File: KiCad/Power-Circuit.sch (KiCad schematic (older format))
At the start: 12 parts, among them P12 M20-9980346, P24 M20-9980346

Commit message: controller board schematic complete
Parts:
- gave numbers to parts that had none: 10
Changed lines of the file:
@@
 $Descr A4 11693 8268
 encoding utf-8
-Sheet 5 5
+Sheet 5 6
 Title ""
 Date ""
@@
 MainsLive
 $Comp
-L FUSE F?
+L FUSE F1
 U 1 1 5682385A
 P 2850 2500
-F 0 "F?" H 2850 2650 50  0000 C CNN
+F 0 "F1" H 2850 2650 50  0000 C CNN
 F 1 "83100000005" H 2850 2350 50  0000 C CNN
 F 2 "" H 2850 2500 50  0000 C CNN
@@
 $EndComp
 $Comp
-L VPP24-830 T?
+L VPP24-830 T1
 U 1 1 568240FC
 P 2900 4400
-F 0 "T?" H 2900 5125 50  0000 C CNN
+F 0 "T1" H 2900 5125 50  0000 C CNN
 F 1 "VPP24-830" H 2900 5025 50  0000 C CNN
 F 2 "" H 2900 4700 50  0000 C CNN
@@
 	2100 4900 2500 4900
 $Comp
-L GND #PWR?
+L GND #PWR29
 U 1 1 56824495
 P 2100 5100
-F 0 "#PWR?" H 2100 4850 50  0001 C CNN
+F 0 "#PWR29" H 2100 4850 50  0001 C CNN
 F 1 "GND" H 2100 4950 50  0000 C CNN
 F 2 "" H 2100 5100 50  0000 C CNN
@@
 	5350 4900 5350 4650
 $Comp
-L R R?
+L R R24
 U 1 1 56825401
 P 5750 4400
-F 0 "R?" V 5830 4400 50  0000 C CNN
+F 0 "R24" V 5830 4400 50  0000 C CNN
 F 1 "R" V 5750 4400 50  0000 C CNN
 F 2 "" V 5680 4400 50  0000 C CNN
@@
 $EndComp
 $Comp
-L +12V #PWR?
+L +12V #PWR32
 U 1 1 56825633
 P 5950 4650
-F 0 "#PWR?" H 5950 4500 50  0001 C CNN
+F 0 "#PWR32" H 5950 4500 50  0001 C CNN
 F 1 "+12V" H 5950 4790 50  0000 C CNN
 F 2 "" H 5950 4650 50  0000 C CNN
@@
 $EndComp
 $Comp
-L VCC #PWR?
+L VCC #PWR31
 U 1 1 56825671
 P 5950 4150
-F 0 "#PWR?" H 5950 4000 50  0001 C CNN
+F 0 "#PWR31" H 5950 4000 50  0001 C CNN
 F 1 "VCC" H 5950 4300 50  0000 C CNN
 F 2 "" H 5950 4150 50  0000 C CNN
@@
 Connection ~ 5750 4650
 $Comp
-L FUSE F?
+L FUSE F2
 U 1 1 56825CC3
 P 6350 3900
-F 0 "F?" H 6350 4150 50  0000 C CNN
+F 0 "F2" H 6350 4150 50  0000 C CNN
 F 1 "83100000005" H 6350 4050 50  0000 C CNN
 F 2 "" H 6350 3900 50  0000 C CNN
@@
 Connection ~ 5350 4900
 $Comp
-L GND #PWR?
+L GND #PWR33
 U 1 1 5682607E
 P 6400 4550
-F 0 "#PWR?" H 6400 4300 50  0001 C CNN
+F 0 "#PWR33" H 6400 4300 50  0001 C CNN
 F 1 "GND" H 6400 4400 50  0000 C CNN
 F 2 "" H 6400 4550 50  0000 C CNN
@@
 	6400 4400 6400 4550
 $Comp
-L DF04M D?
+L DF04M D2
 U 1 1 5682669A
 P 7000 4400
-F 0 "D?" H 6750 4700 50  0000 C CNN
+F 0 "D2" H 6750 4700 50  0000 C CNN
 F 1 "DF04M" H 7200 4000 50  0000 C CNN
 F 2 "" H 7000 4400 50  0000 C CNN
@@
 $EndComp
 $Comp
-L VAA #PWR?
+L VAA #PWR30
 U 1 1 56827A47
 P 3500 2500
-F 0 "#PWR?" H 3500 2350 50  0001 C CNN
+F 0 "#PWR30" H 3500 2350 50  0001 C CNN
 F 1 "VAA" V 3500 2650 100 0000 L CNN
 F 2 "" H 3500 2500 50  0000 C CNN
@@
 Connection ~ 2300 2500
 $Comp
-L CP1 C?
+L CP1 C2
 U 1 1 5682AC61
 P 7700 4650
-F 0 "C?" H 7725 4750 50  0000 L CNN
+F 0 "C2" H 7725 4750 50  0000 L CNN
 F 1 ">16.6 mF" H 7725 4550 50  0000 L CNN
 F 2 "" H 7700 4650 50  0000 C CNN
@@
 $EndComp
 $Comp
-L VCC #PWR?
+L VCC #PWR34
 U 1 1 5682B366
 P 7700 4150
-F 0 "#PWR?" H 7700 4000 50  0001 C CNN
+F 0 "#PWR34" H 7700 4000 50  0001 C CNN
 F 1 "VCC" H 7700 4350 100 0000 C CNN
 F 2 "" H 7700 4150 50  0000 C CNN
@@
 $EndComp
 $Comp
-L 7805 U?
+L 7805 U5
 U 1 1 5682B5F4
 P 9350 4450
-F 0 "U?" H 9500 4254 50  0000 C CNN
+F 0 "U5" H 9500 4254 50  0000 C CNN
 F 1 "LM78M05CT" H 9350 4650 50  0000 C CNN
 F 2 "" H 9350 4450 50  0000 C CNN
@@
 $EndComp
 $Comp
-L VDD #PWR?
+L VDD #PWR36
 U 1 1 5682B82F
 P 10200 4400
-F 0 "#PWR?" H 10200 4250 50  0001 C CNN
+F 0 "#PWR36" H 10200 4250 50  0001 C CNN
 F 1 "VDD" V 10200 4550 100 0000 L CNN
 F 2 "" H 10200 4400 50  0000 C CNN
@@
 $EndComp
 $Comp
-L GND #PWR?
+L GND #PWR35
 U 1 1 5682BC67
 P 9350 4950
-F 0 "#PWR?" H 9350 4700 50  0001 C CNN
+F 0 "#PWR35" H 9350 4700 50  0001 C CNN
 F 1 "GND" H 9350 4800 50  0000 C CNN
 F 2 "" H 9350 4950 50  0000 C CNN
@@
 $EndComp
 $Comp
-L C C?
+L C C4
 U 1 1 5682C2EA
 P 9950 4650
-F 0 "C?" H 9975 4750 50  0000 L CNN
+F 0 "C4" H 9975 4750 50  0000 L CNN
 F 1 "0.1 uF" H 9975 4550 50  0000 L CNN
 F 2 "" H 9988 4500 50  0000 C CNN
@@
 $EndComp
 $Comp
-L C C?
+L C C3
 U 1 1 5682CBEE
 P 8750 4650
-F 0 "C?" H 8775 4750 50  0000 L CNN
+F 0 "C3" H 8775 4750 50  0000 L CNN
 F 1 "0.33 uF" H 8775 4550 50  0000 L CNN
 F 2 "" H 8788 4500 50  0000 C CNN
@@
 $EndComp
 $Comp
-L R R?
+L R R25
 U 1 1 5682CEE6
 P 8400 4400
-F 0 "R?" V 8200 4400 50  0000 C CNN
+F 0 "R25" V 8200 4400 50  0000 C CNN
 F 1 "10 Ohm; >= 2W" V 8300 4400 50  0000 C CNN
 F 2 "" V 8330 4400 50  0000 C CNN

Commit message: motor driver design
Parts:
- R24: value R -> 330; footprint (none) -> Resistors_ThroughHole:Resistor_Horizontal_RM10mm
- R25: footprint (none) -> Resistors_ThroughHole:Resistor_Horizontal_RM15mm
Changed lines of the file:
@@
 P 5750 4400
 F 0 "R24" V 5830 4400 50  0000 C CNN
-F 1 "R" V 5750 4400 50  0000 C CNN
-F 2 "" V 5680 4400 50  0001 C CNN
+F 1 "330" V 5750 4400 50  0000 C CNN
+F 2 "Resistors_ThroughHole:Resistor_Horizontal_RM10mm" V 5680 4400 50  0001 C CNN
 F 3 "" H 5750 4400 50  0000 C CNN
 	1    5750 4400
@@
 F 0 "R25" V 8200 4400 50  0000 C CNN
 F 1 "10 Ohm; >= 2W" V 8300 4400 50  0000 C CNN
-F 2 "" V 8330 4400 50  0001 C CNN
+F 2 "Resistors_ThroughHole:Resistor_Horizontal_RM15mm" V 8330 4400 50  0001 C CNN
 F 3 "" H 8400 4400 50  0000 C CNN
 	1    8400 4400

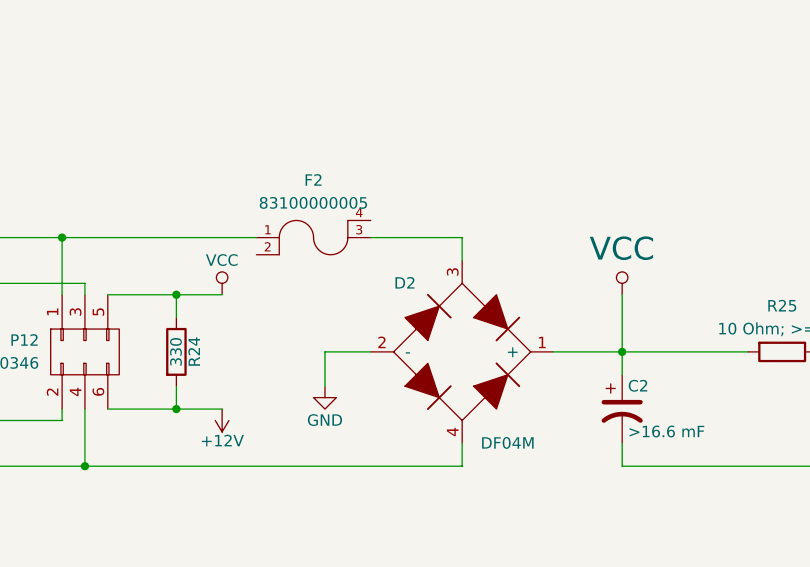
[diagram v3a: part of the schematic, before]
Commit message: capacitors and diode part associations
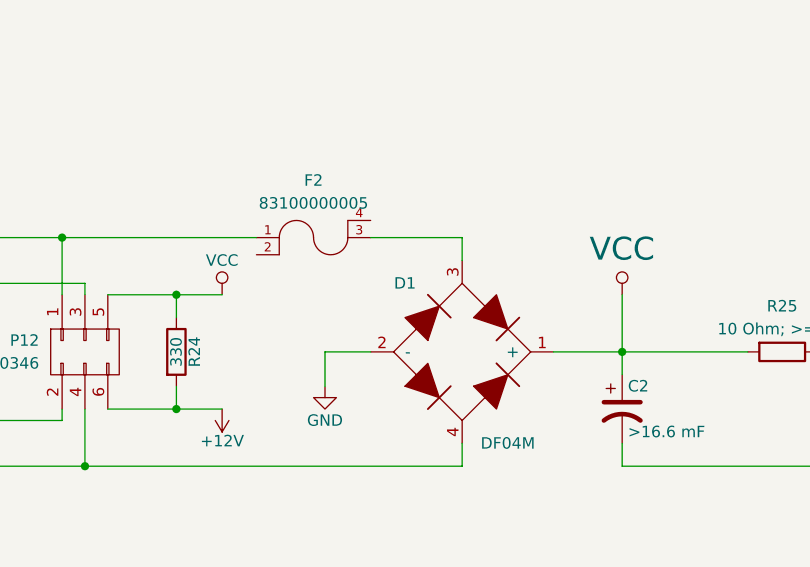
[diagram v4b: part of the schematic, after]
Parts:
- C2: footprint (none) -> Capacitors_ThroughHole:C_Radial_D35_L51_P10
- C3: footprint (none) -> Capacitors_ThroughHole:C_Disc_D6_P5
- C4: footprint (none) -> Capacitors_ThroughHole:C_Disc_D3_P2.5
- D1: renamed from D2; footprint (none) -> Easy-PCB-footprints:DF04M
- P12, P24: footprint (none) -> Easy-PCB-footprints:Male_Header_2x03
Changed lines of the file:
@@
 $Descr A4 11693 8268
 encoding utf-8
-Sheet 5 6
+Sheet 4 6
 Title ""
 Date ""
@@
 F 0 "P24" V 4300 4600 50  0000 L CNN
 F 1 "M20-9980346" V 4400 4600 50  0000 L CNN
-F 2 "" H 4350 3200 50  0001 C CNN
+F 2 "Easy-PCB-footprints:Male_Header_2x03" H 4350 3200 50  0001 C CNN
 F 3 "" H 4350 3200 50  0000 C CNN
 	1    4350 4400
@@
 F 0 "P12" V 5300 4600 50  0000 L CNN
 F 1 "M20-9980346" V 5400 4600 50  0000 L CNN
-F 2 "" H 5350 3200 50  0001 C CNN
+F 2 "Easy-PCB-footprints:Male_Header_2x03" H 5350 3200 50  0001 C CNN
 F 3 "" H 5350 3200 50  0000 C CNN
 	1    5350 4400
@@
 	6400 4400 6400 4550
 $Comp
-L DF04M D2
+L DF04M D1
 U 1 1 5682669A
 P 7000 4400
-F 0 "D2" H 6750 4700 50  0000 C CNN
+F 0 "D1" H 6750 4700 50  0000 C CNN
 F 1 "DF04M" H 7200 4000 50  0000 C CNN
-F 2 "" H 7000 4400 50  0001 C CNN
+F 2 "Easy-PCB-footprints:DF04M" H 7000 4400 50  0001 C CNN
 F 3 "" H 7000 4400 50  0000 C CNN
 	1    7000 4400
@@
 F 0 "C2" H 7725 4750 50  0000 L CNN
 F 1 ">16.6 mF" H 7725 4550 50  0000 L CNN
-F 2 "" H 7700 4650 50  0001 C CNN
+F 2 "Capacitors_ThroughHole:C_Radial_D35_L51_P10" H 7700 4650 50  0001 C CNN
 F 3 "" H 7700 4650 50  0000 C CNN
 	1    7700 4650
@@
 F 0 "C4" H 9975 4750 50  0000 L CNN
 F 1 "0.1 uF" H 9975 4550 50  0000 L CNN
-F 2 "" H 9988 4500 50  0001 C CNN
+F 2 "Capacitors_ThroughHole:C_Disc_D3_P2.5" H 9988 4500 50  0001 C CNN
 F 3 "" H 9950 4650 50  0000 C CNN
 	1    9950 4650
@@
 F 0 "C3" H 8775 4750 50  0000 L CNN
 F 1 "0.33 uF" H 8775 4550 50  0000 L CNN
-F 2 "" H 8788 4500 50  0001 C CNN
+F 2 "Capacitors_ThroughHole:C_Disc_D6_P5" H 8788 4500 50  0001 C CNN
 F 3 "" H 8750 4650 50  0000 C CNN
 	1    8750 4650

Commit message: IC BOM and footprints complete
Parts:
- U5: footprint (none) -> Easy-PCB-footprints:TO-220
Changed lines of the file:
@@
 F 0 "U5" H 9500 4254 50  0000 C CNN
 F 1 "LM78M05CT" H 9350 4650 50  0000 C CNN
-F 2 "" H 9350 4450 50  0001 C CNN
+F 2 "Easy-PCB-footprints:TO-220" H 9350 4450 50  0001 C CNN
 F 3 "" H 9350 4450 50  0000 C CNN
 	1    9350 4450

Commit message: footprint associations complete
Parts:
- F1, F2: footprint (none) -> Easy-PCB-footprints:83100000005_Fuse_Holder
- T1: footprint (none) -> Easy-PCB-footprints:VPP24-830
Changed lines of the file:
@@
 F 0 "F1" H 2850 2650 50  0000 C CNN
 F 1 "83100000005" H 2850 2350 50  0000 C CNN
-F 2 "" H 2850 2500 50  0001 C CNN
+F 2 "Easy-PCB-footprints:83100000005_Fuse_Holder" H 2850 2500 50  0001 C CNN
 F 3 "" H 2850 2500 50  0000 C CNN
 	1    2850 2500
@@
 F 0 "T1" H 2900 5125 50  0000 C CNN
 F 1 "VPP24-830" H 2900 5025 50  0000 C CNN
-F 2 "" H 2900 4700 50  0001 C CNN
+F 2 "Easy-PCB-footprints:VPP24-830" H 2900 4700 50  0001 C CNN
 F 3 "" H 2900 4700 50  0000 C CNN
 	1    2900 4400
@@
 F 0 "F2" H 6350 4150 50  0000 C CNN
 F 1 "83100000005" H 6350 4050 50  0000 C CNN
-F 2 "" H 6350 3900 50  0001 C CNN
+F 2 "Easy-PCB-footprints:83100000005_Fuse_Holder" H 6350 3900 50  0001 C CNN
 F 3 "" H 6350 3900 50  0000 C CNN
 	1    6350 3900

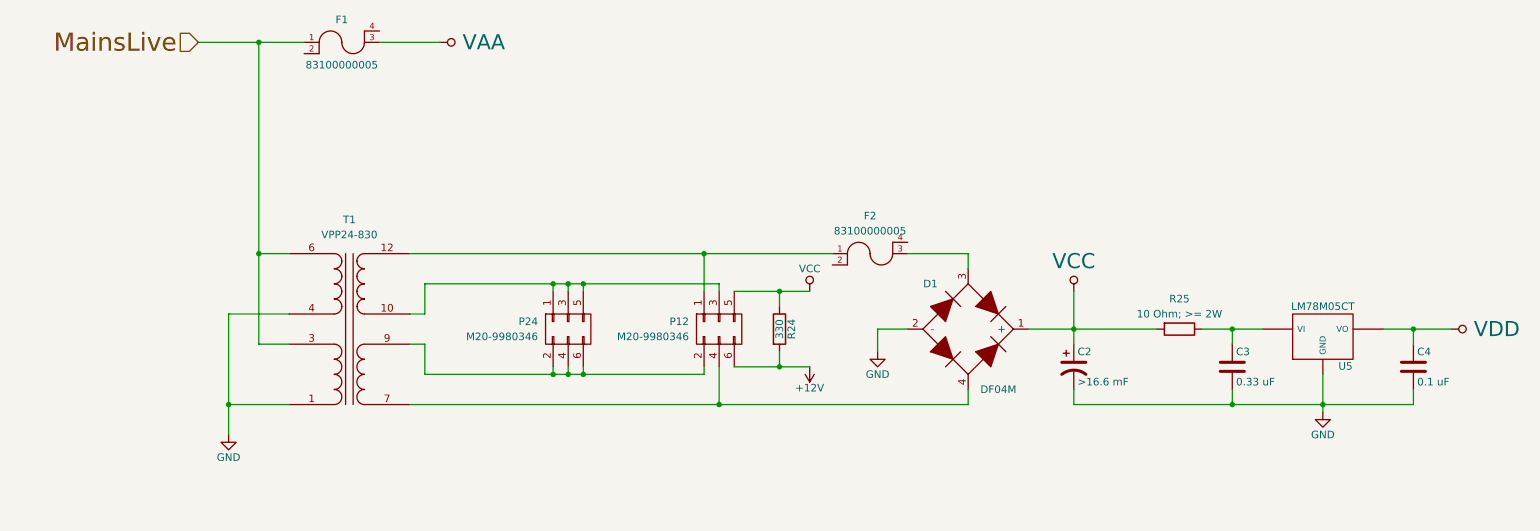
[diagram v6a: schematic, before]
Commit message: errors cleared and components on board
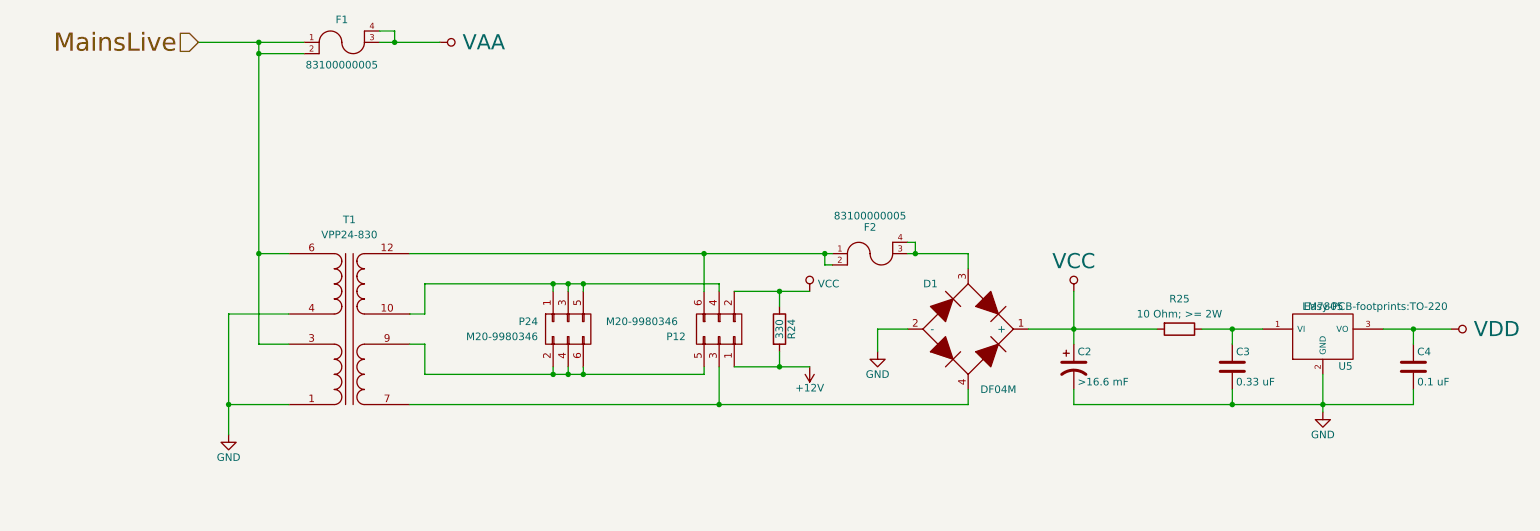
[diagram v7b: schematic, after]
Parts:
- removed U5: LM78M05CT, Easy-PCB-footprints:TO-220, symbol 7805
- added U5: LM7805, Easy-PCB-footprints:TO-220, symbol LM7805
- C2: footprint Capacitors_ThroughHole:C_Radial_D35_L51_P10 -> Easy-PCB-footprints:C_Radial_D35_L51_P10
- C3: footprint Capacitors_ThroughHole:C_Disc_D6_P5 -> Easy-PCB-footprints:C_Disc_D6_P5
- C4: footprint Capacitors_ThroughHole:C_Disc_D3_P2.5 -> Easy-PCB-footprints:C_Disc_D3_P2.5
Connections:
- net +12V: now also P12.1 (P1); no longer P12.6 (P6)
- net GND: now also U5.2 (GND)
- net MainsLive: now also F1.2
- net VAA: now also F1.4
- net VCC: now also P12.2 (P2); no longer P12.5 (P5)
- net VDD: now also U5.3 (VO)
- net at P24.1 (P1), P24.3 (P3), P24.5 (P5)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: now also P12.4 (P4); no longer P12.3 (P3)
- net at F2.1, T1.12 (SD): now also F2.2, P12.6 (P6); no longer P12.1 (P1)
- net at D1.4, T1.7 (SA): now also P12.3 (P3); no longer P12.4 (P4)
- net at P24.2 (P2), P24.4 (P4), P24.6 (P6)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: now also P12.5 (P5); no longer P12.2 (P2)
- net at D1.3, F2.3: now also F2.4
- net at C3.1, R25.1: now also U5.1 (VI)
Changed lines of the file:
@@
 U 1 1 5682471A
 P 5350 4400
-F 0 "P12" V 5300 4600 50  0000 L CNN
-F 1 "M20-9980346" V 5400 4600 50  0000 L CNN
+F 0 "P12" V 5300 4050 50  0000 L CNN
+F 1 "M20-9980346" V 5400 3650 50  0000 L CNN
 F 2 "Easy-PCB-footprints:Male_Header_2x03" H 5350 3200 50  0001 C CNN
 F 3 "" H 5350 3200 50  0000 C CNN
 	1    5350 4400
-	0    -1   1    0
+	0    1    -1   0
 $EndComp
 Wire Wire Line
@@
 P 5950 4150
 F 0 "#PWR031" H 5950 4000 50  0001 C CNN
-F 1 "VCC" H 5950 4300 50  0000 C CNN
+F 1 "VCC" H 6075 4200 50  0000 C CNN
 F 2 "" H 5950 4150 50  0000 C CNN
 F 3 "" H 5950 4150 50  0000 C CNN
@@
 	5750 4550 5750 4650
 Connection ~ 5750 4650
-$Comp
-L FUSE F2
-U 1 1 56825CC3
-P 6350 3900
-F 0 "F2" H 6350 4150 50  0000 C CNN
-F 1 "83100000005" H 6350 4050 50  0000 C CNN
-F 2 "Easy-PCB-footprints:83100000005_Fuse_Holder" H 6350 3900 50  0001 C CNN
-F 3 "" H 6350 3900 50  0000 C CNN
-	1    6350 3900
-	1    0    0    -1
-$EndComp
 Connection ~ 5250 3900
 Wire Wire Line
@@
 F 0 "C2" H 7725 4750 50  0000 L CNN
 F 1 ">16.6 mF" H 7725 4550 50  0000 L CNN
-F 2 "Capacitors_ThroughHole:C_Radial_D35_L51_P10" H 7700 4650 50  0001 C CNN
+F 2 "Easy-PCB-footprints:C_Radial_D35_L51_P10" H 7700 4650 50  0001 C CNN
 F 3 "" H 7700 4650 50  0000 C CNN
 	1    7700 4650
@@
 F 3 "" H 7700 4150 50  0000 C CNN
 	1    7700 4150
-	1    0    0    -1
-$EndComp
-$Comp
-L 7805 U5
-U 1 1 5682B5F4
-P 9350 4450
-F 0 "U5" H 9500 4254 50  0000 C CNN
-F 1 "LM78M05CT" H 9350 4650 50  0000 C CNN
-F 2 "Easy-PCB-footprints:TO-220" H 9350 4450 50  0001 C CNN
-F 3 "" H 9350 4450 50  0000 C CNN
-	1    9350 4450
 	1    0    0    -1
 $EndComp
@@
 F 0 "C4" H 9975 4750 50  0000 L CNN
 F 1 "0.1 uF" H 9975 4550 50  0000 L CNN
-F 2 "Capacitors_ThroughHole:C_Disc_D3_P2.5" H 9988 4500 50  0001 C CNN
+F 2 "Easy-PCB-footprints:C_Disc_D3_P2.5" H 9988 4500 50  0001 C CNN
 F 3 "" H 9950 4650 50  0000 C CNN
 	1    9950 4650
@@
 F 0 "C3" H 8775 4750 50  0000 L CNN
 F 1 "0.33 uF" H 8775 4550 50  0000 L CNN
-F 2 "Capacitors_ThroughHole:C_Disc_D6_P5" H 8788 4500 50  0001 C CNN
+F 2 "Easy-PCB-footprints:C_Disc_D6_P5" H 8788 4500 50  0001 C CNN
 F 3 "" H 8750 4650 50  0000 C CNN
 	1    8750 4650
@@
 	9350 4700 9350 4950
 Connection ~ 9350 4900
+$Comp
+L LM7805 U5
+U 1 1 56895B8F
+P 9350 4450
+F 0 "U5" H 9500 4254 50  0000 C CNN
+F 1 "LM7805" H 9350 4650 50  0000 C CNN
+F 2 "Easy-PCB-footprints:TO-220" H 9700 4650 50  0000 C CNN
+F 3 "" H 9350 4450 50  0000 C CNN
+	1    9350 4450
+	1    0    0    -1
+$EndComp
+$Comp
+L FUSE F2
+U 1 1 5689B1E0
+P 6350 3900
+F 0 "F2" H 6350 4075 50  0000 C CNN
+F 1 "83100000005" H 6350 4150 50  0000 C CNN
+F 2 "Easy-PCB-footprints:83100000005_Fuse_Holder" H 6350 3900 50  0001 C CNN
+F 3 "" H 6350 3900 50  0000 C CNN
+	1    6350 3900
+	1    0    0    -1
+$EndComp
+Wire Wire Line
+	2600 2575 2300 2575
+Connection ~ 2300 2575
+Wire Wire Line
+	3100 2425 3200 2425
+Wire Wire Line
+	3200 2425 3200 2500
+Connection ~ 3200 2500
+Wire Wire Line
+	6050 3900 6050 3975
+Wire Wire Line
+	6050 3975 6100 3975
+Connection ~ 6050 3900
+Wire Wire Line
+	6650 3900 6650 3825
+Wire Wire Line
+	6650 3825 6600 3825
+Connection ~ 6650 3900
 $EndSCHEMATC

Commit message: power supply placed and routed
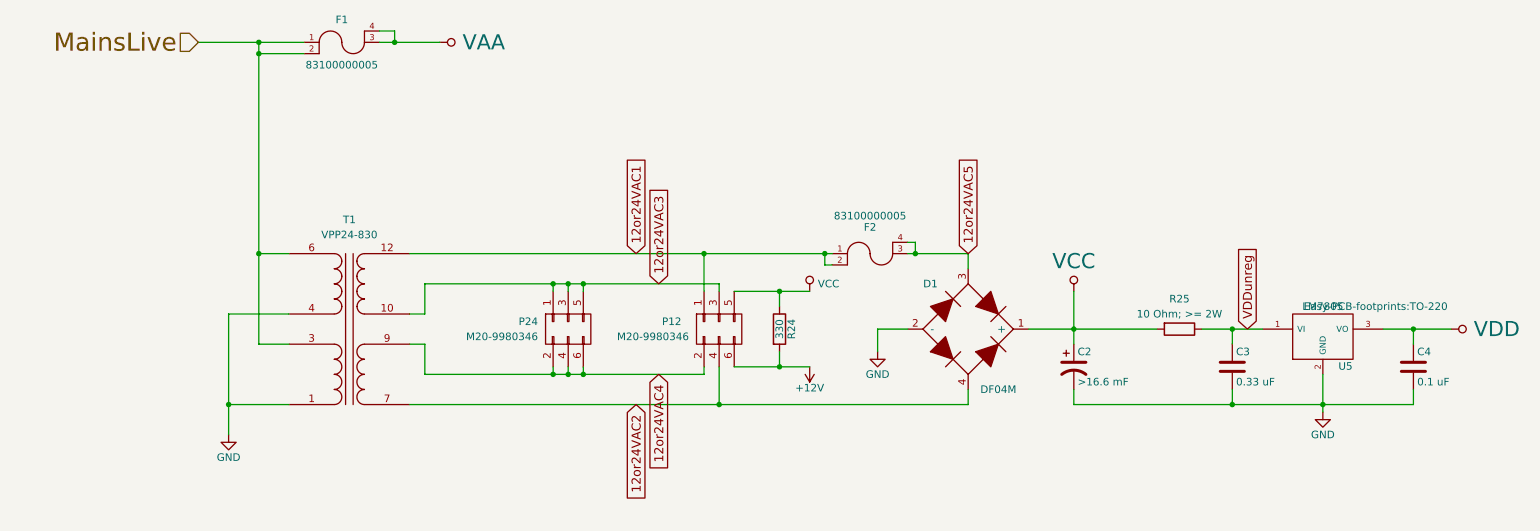
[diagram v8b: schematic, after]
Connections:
- net +12V: now also P12.6 (P6); no longer P12.1 (P1)
- net VCC: now also P12.5 (P5); no longer P12.2 (P2)
- net 12or24VAC3: now reaches P24.1 (P1), P24.3 (P3), P24.5 (P5), T1.10 (SC)
- net 12or24VAC3: now also P12.3 (P3); no longer P12.4 (P4)
- net 12or24VAC1: now reaches F2.1, F2.2, T1.12 (SD)
- net 12or24VAC1: now also P12.1 (P1); no longer P12.6 (P6)
- net 12or24VAC2: now reaches D1.4, T1.7 (SA)
- net 12or24VAC2: now also P12.4 (P4); no longer P12.3 (P3)
- net 12or24VAC4: now reaches P24.2 (P2), P24.4 (P4), P24.6 (P6), T1.9 (SB)
- net 12or24VAC4: now also P12.2 (P2); no longer P12.5 (P5)
- net 12or24VAC5: now reaches D1.3, F2.3, F2.4
- net VDDunreg: now reaches C3.1, R25.1, U5.1 (VI)
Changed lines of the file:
@@
 U 1 1 5682471A
 P 5350 4400
-F 0 "P12" V 5300 4050 50  0000 L CNN
-F 1 "M20-9980346" V 5400 3650 50  0000 L CNN
+F 0 "P12" V 5300 4650 50  0000 L CNN
+F 1 "M20-9980346" V 5400 4600 50  0000 L CNN
 F 2 "Easy-PCB-footprints:Male_Header_2x03" H 5350 3200 50  0001 C CNN
 F 3 "" H 5350 3200 50  0000 C CNN
 	1    5350 4400
-	0    1    -1   0
+	0    -1   1    0
 $EndComp
 Wire Wire Line
@@
 	6650 3825 6600 3825
 Connection ~ 6650 3900
+Text GLabel 4800 3900 1    60   Input ~ 0
+12or24VAC1
+Text GLabel 4800 4900 3    60   Input ~ 0
+12or24VAC2
+Text GLabel 4950 4100 1    60   Input ~ 0
+12or24VAC3
+Text GLabel 4950 4700 3    60   Input ~ 0
+12or24VAC4
+Text GLabel 7000 3900 1    60   Input ~ 0
+12or24VAC5
+Text GLabel 8850 4400 1    60   Input ~ 0
+VDDunreg
 $EndSCHEMATC
